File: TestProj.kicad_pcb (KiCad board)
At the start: 2 copper layers, 24 parts, among them SW1 SW_Push, U1 ATmega32U4-AU, Y1 16MHz

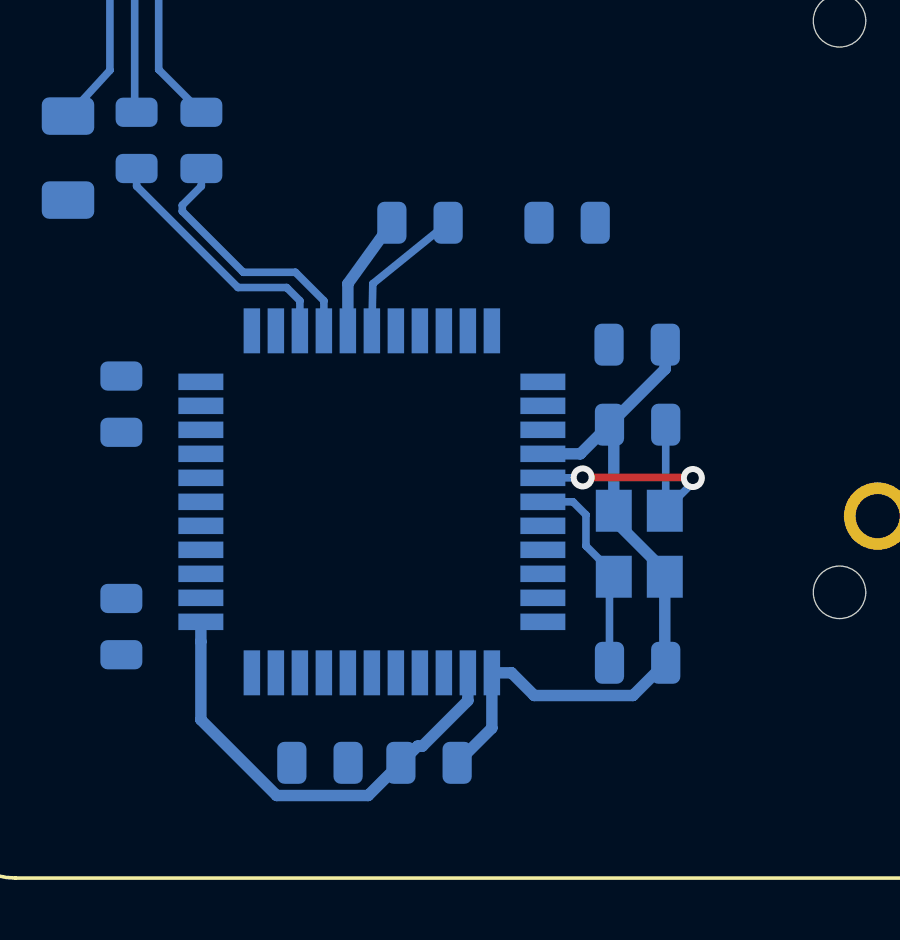
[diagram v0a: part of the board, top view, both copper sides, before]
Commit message: early pcb routing
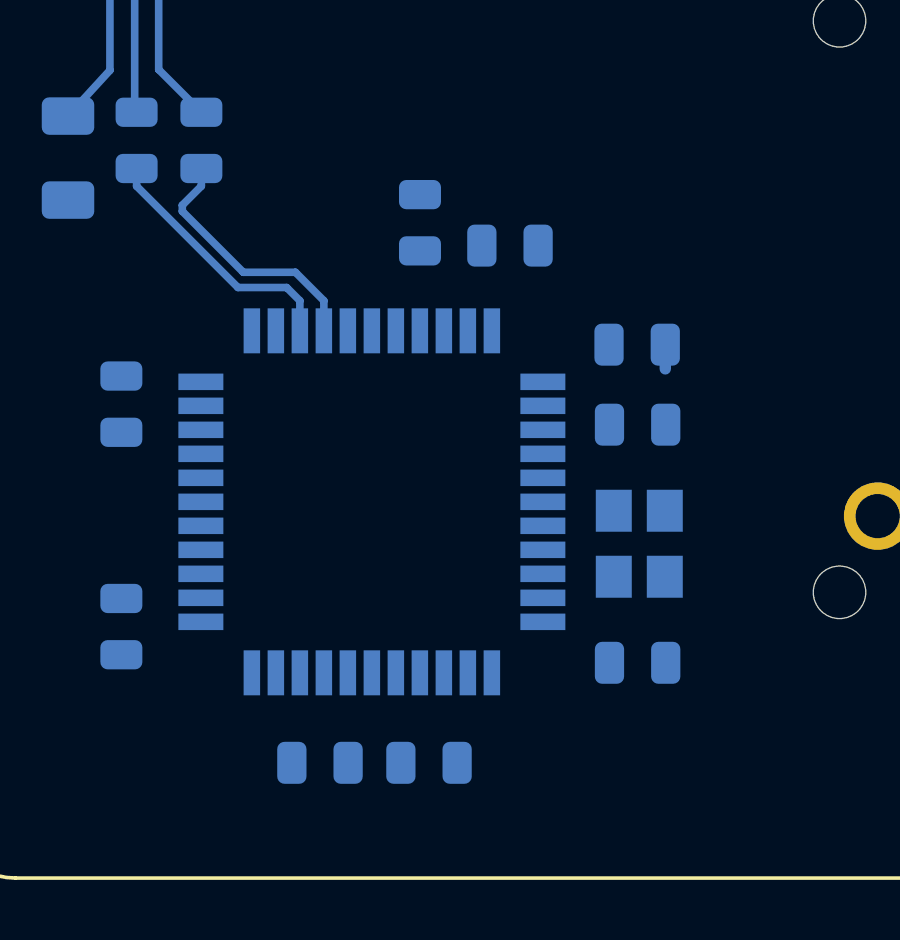
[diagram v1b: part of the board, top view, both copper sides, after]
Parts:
- moved R3 2.05 mm to (106.2, 105.9)
- turned C7 to 90 degrees
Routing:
- net GND: track 28.9 -> 1.55 mm
- net +5V: track 15.4 -> 0.00 mm
- net Net-(C4-Pad1): track 9.37 -> 0.04 mm, vias 2 -> 0
- net Net-(C3-Pad1): track 6.99 -> 0.30 mm
- net Net-(C7-Pad1): track 4.80 -> 0.00 mm
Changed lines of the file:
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@@
     (thickness 1.6)
     (drawings 8)
-    (tracks 67)
+    (tracks 28)
     (zones 0)
     (modules 24)
@@
   )
   (module Resistor_SMD:R_0805_2012Metric (layer B.Cu)
-    (at 108.077 105.156 180)
+    (at 106.172 105.918 180)
     (descr "Resistor SMD 0805 (2012 Metric), square (rectangular) end terminal, IPC_7351 nominal, (Body size source: https://docs.google.com/spreadsheets/d/1BsfQQcO9C6DZCsRaXUlFlo91Tg2WpOkGARC1WS5S8t0/edit?usp=sharing), generated with kicad-footprint-generator")
     (tags resistor)
@@
   )
   (module Capacitor_SMD:C_0805_2012Metric (layer B.Cu)
-    (at 103.1725 105.156 180)
+    (at 103.1725 105.156 90)
     (descr "Capacitor SMD 0805 (2012 Metric), square (rectangular) end terminal, IPC_7351 nominal, (Body size source: https://docs.google.com/spreadsheets/d/1BsfQQcO9C6DZCsRaXUlFlo91Tg2WpOkGARC1WS5S8t0/edit?usp=sharing), generated with kicad-footprint-generator")
     (tags capacitor)
     (attr smd)
-    (fp_text reference C7 (at 0 1.65) (layer B.SilkS)
-      (effects (font (size 1 1) (thickness 0.15)) (justify mirror))
-    )
-    (fp_text value 1uF (at 0 -1.65) (layer B.Fab)
-      (effects (font (size 1 1) (thickness 0.15)) (justify mirror))
-    )
-    (fp_text user %R (at 0 0) (layer B.Fab)
+    (fp_text reference C7 (at 0 1.65 90) (layer B.SilkS)
+      (effects (font (size 1 1) (thickness 0.15)) (justify mirror))
+    )
+    (fp_text value 1uF (at 0 -1.65 90) (layer B.Fab)
+      (effects (font (size 1 1) (thickness 0.15)) (justify mirror))
+    )
+    (fp_text user %R (at 0 0 90) (layer B.Fab)
       (effects (font (size 0.5 0.5) (thickness 0.08)) (justify mirror))
     )
@@
     (fp_line (start -1 0.6) (end 1 0.6) (layer B.Fab) (width 0.1))
     (fp_line (start -1 -0.6) (end -1 0.6) (layer B.Fab) (width 0.1))
-    (pad 2 smd roundrect (at 0.9375 0 180) (size 0.975 1.4) (layers B.Cu B.Paste B.Mask) (roundrect_rratio 0.25)
-      (net 1 GND))
-    (pad 1 smd roundrect (at -0.9375 0 180) (size 0.975 1.4) (layers B.Cu B.Paste B.Mask) (roundrect_rratio 0.25)
+    (pad 2 smd roundrect (at 0.9375 0 90) (size 0.975 1.4) (layers B.Cu B.Paste B.Mask) (roundrect_rratio 0.25)
+      (net 1 GND))
+    (pad 1 smd roundrect (at -0.9375 0 90) (size 0.975 1.4) (layers B.Cu B.Paste B.Mask) (roundrect_rratio 0.25)
       (net 5 "Net-(C7-Pad1)"))
     (model ${KISYS3DMOD}/Capacitor_SMD.3dshapes/C_0805_2012Metric.wrl
@@
   (gr_arc (start 148.43125 124.61875) (end 148.43125 127) (angle -90) (layer F.SilkS) (width 0.12))
   (gr_arc (start 148.43125 91.28125) (end 150.8125 91.28125) (angle -90) (layer F.SilkS) (width 0.12))
-  (segment (start 100.76825 107.188) (end 100.76825 108.75875) (width 0.381) (layer B.Cu) (net 1))
-  (segment (start 102.235 105.156) (end 100.76825 107.188) (width 0.381) (layer B.Cu) (net 1))
-  (segment (start 109.63275 115.058652) (end 111.33275 116.758652) (width 0.381) (layer B.Cu) (net 1))
   (segment (start 111.33275 116.758652) (end 111.33275 116.95575) (width 0.381) (layer B.Cu) (net 1))
   (segment (start 109.63275 114.75575) (end 109.63275 115.058652) (width 0.381) (layer B.Cu) (net 1))
   (segment (start 109.63275 112.03075) (end 109.489 111.887) (width 0.381) (layer B.Cu) (net 1))
-  (segment (start 109.63275 114.75575) (end 109.63275 112.03075) (width 0.381) (layer B.Cu) (net 1))
-  (segment (start 108.51725 112.85875) (end 107.26825 112.85875) (width 0.381) (layer B.Cu) (net 1))
-  (segment (start 109.489 111.887) (end 108.51725 112.85875) (width 0.381) (layer B.Cu) (net 1))
-  (segment (start 111.349 110.027) (end 109.489 111.887) (width 0.381) (layer B.Cu) (net 1))
   (segment (start 111.349 109.22) (end 111.349 110.027) (width 0.381) (layer B.Cu) (net 1))
   (segment (start 111.33275 119.79325) (end 111.364 119.8245) (width 0.381) (layer B.Cu) (net 1))
-  (segment (start 111.33275 116.95575) (end 111.33275 119.79325) (width 0.381) (layer B.Cu) (net 1))
-  (segment (start 106.22425 120.15875) (end 105.56825 120.15875) (width 0.381) (layer B.Cu) (net 1))
-  (segment (start 106.98051 120.91501) (end 106.22425 120.15875) (width 0.381) (layer B.Cu) (net 1))
-  (segment (start 110.27349 120.91501) (end 106.98051 120.91501) (width 0.381) (layer B.Cu) (net 1))
-  (segment (start 111.364 119.8245) (end 110.27349 120.91501) (width 0.381) (layer B.Cu) (net 1))
-  (segment (start 105.56825 122.00075) (end 105.56825 120.15875) (width 0.381) (layer B.Cu) (net 1))
-  (segment (start 104.41075 123.15825) (end 105.56825 122.00075) (width 0.381) (layer B.Cu) (net 1))
-  (segment (start 103.091987 122.602013) (end 103.252889 122.602013) (width 0.381) (layer B.Cu) (net 2))
-  (segment (start 104.76825 121.086652) (end 104.76825 120.15875) (width 0.381) (layer B.Cu) (net 2))
-  (segment (start 103.252889 122.602013) (end 104.76825 121.086652) (width 0.381) (layer B.Cu) (net 2))
-  (segment (start 102.53575 123.15825) (end 103.091987 122.602013) (width 0.381) (layer B.Cu) (net 2))
-  (segment (start 95.86825 119.11475) (end 95.86825 118.45875) (width 0.381) (layer B.Cu) (net 2))
-  (segment (start 95.86825 121.72223) (end 95.86825 119.11475) (width 0.381) (layer B.Cu) (net 2))
-  (segment (start 98.39478 124.24876) (end 95.86825 121.72223) (width 0.381) (layer B.Cu) (net 2))
-  (segment (start 101.44524 124.24876) (end 98.39478 124.24876) (width 0.381) (layer B.Cu) (net 2))
-  (segment (start 102.53575 123.15825) (end 101.44524 124.24876) (width 0.381) (layer B.Cu) (net 2))
-  (segment (start 108.705749 115.928749) (end 109.63275 116.85575) (width 0.254) (layer B.Cu) (net 3))
-  (segment (start 108.705749 114.892249) (end 108.705749 115.928749) (width 0.254) (layer B.Cu) (net 3))
-  (segment (start 108.27225 114.45875) (end 108.705749 114.892249) (width 0.254) (layer B.Cu) (net 3))
   (segment (start 109.63275 116.85575) (end 109.63275 116.95575) (width 0.254) (layer B.Cu) (net 3))
-  (segment (start 107.26825 114.45875) (end 108.27225 114.45875) (width 0.254) (layer B.Cu) (net 3))
   (segment (start 109.489 117.0995) (end 109.63275 116.95575) (width 0.254) (layer B.Cu) (net 3))
-  (segment (start 109.489 119.8245) (end 109.489 117.0995) (width 0.254) (layer B.Cu) (net 3))
   (segment (start 111.364 114.7245) (end 111.33275 114.75575) (width 0.254) (layer B.Cu) (net 4))
-  (segment (start 111.364 111.887) (end 111.364 114.7245) (width 0.254) (layer B.Cu) (net 4))
-  (segment (start 108.581664 113.65875) (end 108.594996 113.645418) (width 0.254) (layer B.Cu) (net 4))
-  (via (at 108.594996 113.645418) (size 0.8) (drill 0.4) (layers F.Cu B.Cu) (net 4))
-  (segment (start 107.26825 113.65875) (end 108.581664 113.65875) (width 0.254) (layer B.Cu) (net 4))
-  (via (at 112.268 113.665) (size 0.8) (drill 0.4) (layers F.Cu B.Cu) (net 4))
-  (segment (start 112.248418 113.645418) (end 112.268 113.665) (width 0.254) (layer F.Cu) (net 4))
-  (segment (start 108.594996 113.645418) (end 112.248418 113.645418) (width 0.254) (layer F.Cu) (net 4))
-  (segment (start 112.268 113.8205) (end 111.33275 114.75575) (width 0.254) (layer B.Cu) (net 4))
-  (segment (start 112.268 113.665) (end 112.268 113.8205) (width 0.254) (layer B.Cu) (net 4))
-  (segment (start 101.6 107.188) (end 101.56825 108.75875) (width 0.254) (layer B.Cu) (net 5))
-  (segment (start 104.11 105.156) (end 101.6 107.188) (width 0.254) (layer B.Cu) (net 5))
   (segment (start 92.837 96.6545) (end 92.837 100.076) (width 0.254) (layer B.Cu) (net 12))
   (segment (start 92.8625 96.629) (end 92.837 96.6545) (width 0.254) (layer B.Cu) (net 12))

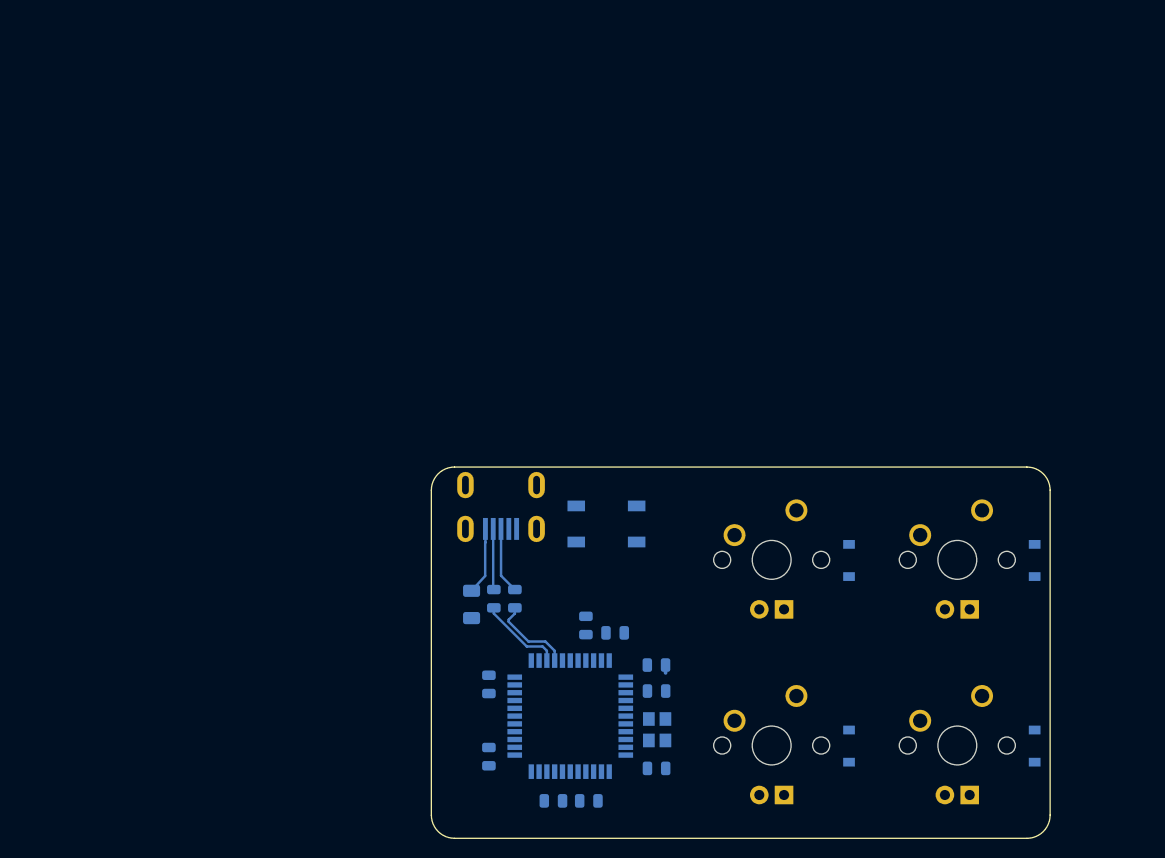
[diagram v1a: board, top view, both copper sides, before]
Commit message: starting from scratch with atmega32u2
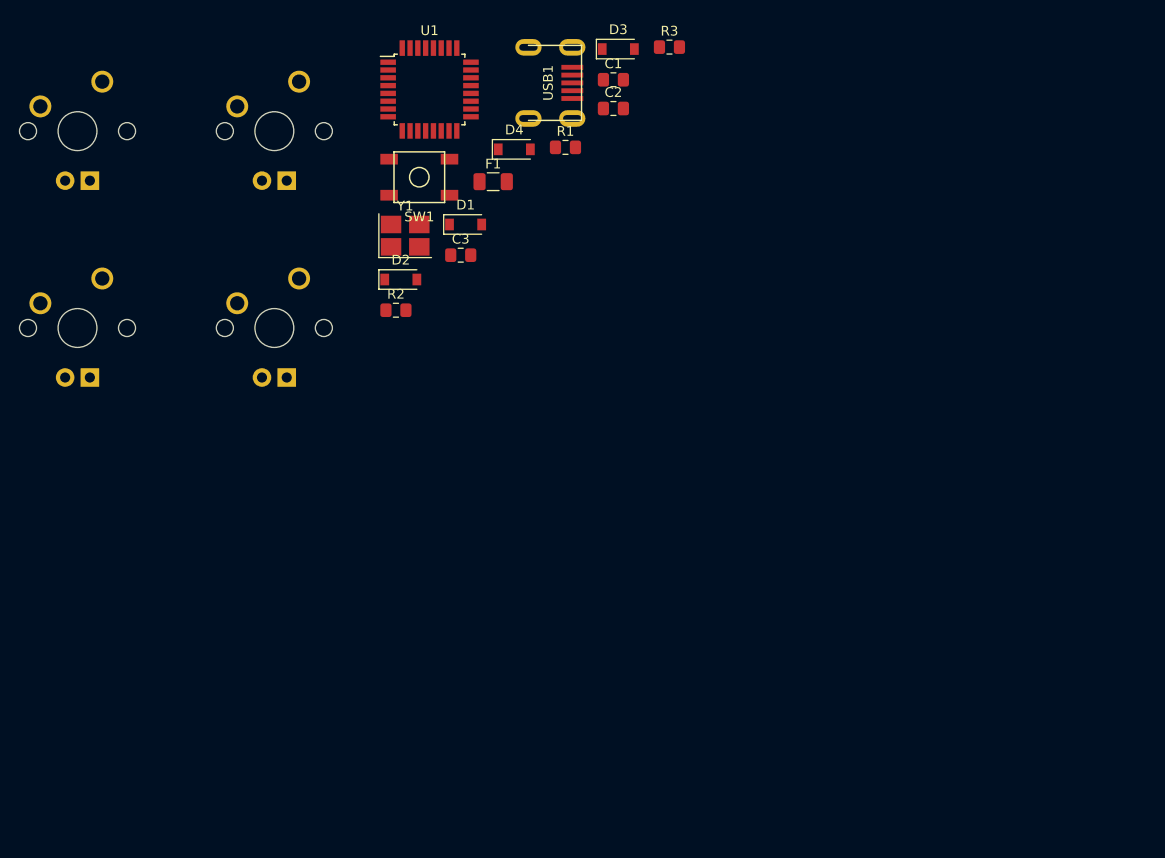
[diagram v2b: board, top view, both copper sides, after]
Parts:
- removed C4: 22pF, Capacitor_SMD:C_0805_2012Metric
- removed C5: 0.1uF, Capacitor_SMD:C_0805_2012Metric
- removed C6: 10uF, Capacitor_SMD:C_0805_2012Metric
- removed C7: 1uF, Capacitor_SMD:C_0805_2012Metric
- removed R4: 10k, Resistor_SMD:R_0805_2012Metric
- C1, C2: value 0.1uF -> 22pF; footprint Capacitor_SMD:C_0805_2012Metric -> Capacitor_SMD:C_0805_2012Metric_Pad1.15x1.40mm_HandSolder; moved to F.Cu
- C3: value 22pF -> 1uF; footprint Capacitor_SMD:C_0805_2012Metric -> Capacitor_SMD:C_0805_2012Metric_Pad1.15x1.40mm_HandSolder; moved to F.Cu
- D1, D2, D3, D4, F1, SW1, USB1: moved to F.Cu
- R1, R2, R3: footprint Resistor_SMD:R_0805_2012Metric -> Resistor_SMD:R_0805_2012Metric_Pad1.15x1.40mm_HandSolder; moved to F.Cu
- U1: value ATmega32U4-AU -> ATmega32U2-AU; footprint Package_QFP:TQFP-44_10x10mm_P0.8mm -> Package_QFP:TQFP-32_7x7mm_P0.8mm; moved to F.Cu
- Y1: footprint Crystal:Crystal_SMD_3225-4Pin_3.2x2.5mm -> Crystal:Crystal_SMD_3225-4Pin_3.2x2.5mm_HandSoldering; moved to F.Cu
- moved MX2 95.1 mm to (51.0, 54.4)
- moved MX3 82.7 mm to (71.2, 54.4)
- moved MX4 82.1 mm to (71.2, 74.6)
- moved D4 81.3 mm to (95.8, 56.3), turned to 0 degrees
- moved MX1 75.1 mm to (51.0, 74.6)
- moved C2 71.1 mm to (106.0, 52.1)
- moved D3 67.7 mm to (106.5, 46.0), turned to 0 degrees
- moved D2 66.4 mm to (84.2, 69.7), turned to 0 degrees
- moved U1 65.9 mm to (87.1, 50.2), turned to 0 degrees
- moved R3 60.4 mm to (111.7, 45.8), turned to 0 degrees
- moved C1 60.2 mm to (106.0, 49.2)
- moved Y1 56.9 mm to (84.6, 65.2), turned to 0 degrees
- moved C3 56.4 mm to (90.3, 67.2)
- moved D1 52.3 mm to (90.8, 64.0), turned to 0 degrees
- moved R1 46.9 mm to (101.1, 56.1), turned to 0 degrees
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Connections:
- C1 pad 1: +5V -> Net-(C1-Pad1)
- C2 pad 1: +5V -> GND
- C2 pad 2: GND -> Net-(C2-Pad2)
- R1 pad 1: Net-(R1-Pad1) -> D-
- R1 pad 2: D- -> Net-(R1-Pad2)
- U1 pad 1: Net-(U1-Pad1) -> Net-(C1-Pad1)
- U1 pad 13: Net-(R3-Pad2) -> Net-(U1-Pad13)
- U1 pad 14: +5V -> Net-(U1-Pad14)
- U1 pad 15: GND -> Net-(U1-Pad15)
- U1 pad 16: Net-(C4-Pad1) -> Net-(U1-Pad16)
- U1 pad 17: Net-(C3-Pad1) -> Net-(U1-Pad17)
- U1 pad 2: +5V -> Net-(C2-Pad2)
- U1 pad 23: GND -> Net-(U1-Pad23)
- U1 pad 24: +5V -> Net-(R3-Pad2)
- U1 pad 27: Net-(U1-Pad27) -> Net-(C3-Pad1)
- U1 pad 28: Net-(U1-Pad28) -> GND
- U1 pad 29: Net-(U1-Pad29) -> Net-(R2-Pad1)
- U1 pad 3: Net-(R1-Pad1) -> GND
- U1 pad 30: Net-(U1-Pad30) -> Net-(R1-Pad2)
- U1 pad 31: Net-(U1-Pad31) -> +5V
- U1 pad 32: Net-(U1-Pad32) -> +5V
- U1 pad 4: Net-(R2-Pad1) -> +5V
- U1 pad 5: GND -> Net-(U1-Pad5)
- U1 pad 7: +5V -> Net-(U1-Pad7)
- Y1 pad 1: Net-(C4-Pad1) -> Net-(C1-Pad1)
- Y1 pad 3: Net-(C3-Pad1) -> Net-(C2-Pad2)
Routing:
- net Net-(R2-Pad1): track 8.65 -> 0.00 mm
- net Net-(R1-Pad1): track 8.62 -> 0.00 mm
- net VCC: track 6.90 -> 0.00 mm
- net D+: track 6.81 -> 0.00 mm
- net D-: track 6.25 -> 0.00 mm
- net GND: track 1.55 -> 0.00 mm

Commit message: a poor routing job 8)
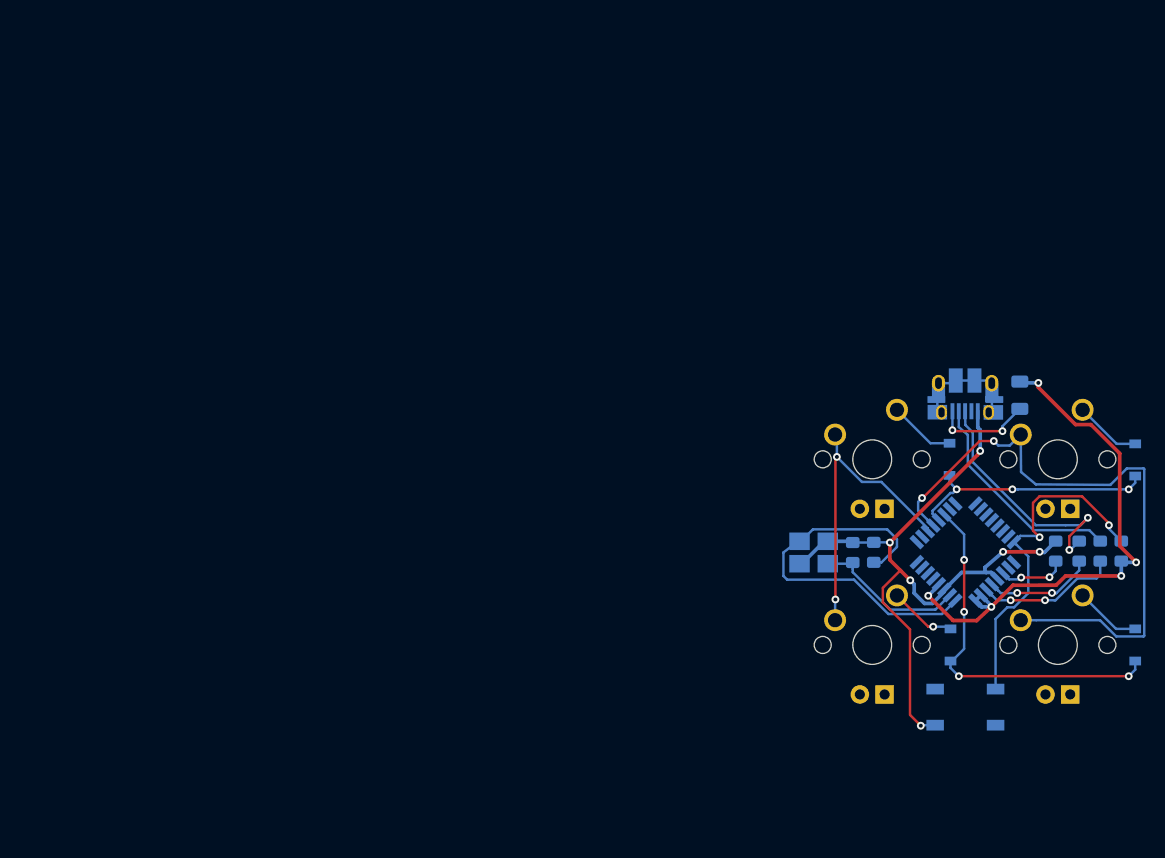
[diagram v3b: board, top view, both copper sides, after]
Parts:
- removed F1: 500mA, Fuse:Fuse_1206_3216Metric
- removed USB1: Molex-0548190589, random-keyboard-parts:Molex-0548190589
- added F2: 500mA, Fuse:Fuse_1206_3216Metric, B.Cu at (147.7, 81.5)
- added J1: USB_B_Micro, Connector_USB:USB_Micro-B_Amphenol_10103594-0001LF_Horizontal, B.Cu at (142.1, 81.4)
- C1, C2, C3, D1, D2, D3, D4, R1, R2, R3, U1, Y1: moved to B.Cu
- SW1: footprint random-keyboard-parts:SKQG-1155865 -> random-keyboard-parts:SKQGADE010; moved to B.Cu
- moved MX2 97.1 mm to (132.6, 107.2)
- moved MX3 87.2 mm to (151.6, 88.1)
- moved MX4 86.7 mm to (151.6, 107.2)
- moved MX1 82.7 mm to (132.6, 88.1)
- moved D4 81.5 mm to (159.5, 107.2), turned to 90 degrees
- moved SW1 78.1 mm to (142.1, 113.5), turned to 180 degrees
- moved R2 74.4 mm to (153.8, 97.5), turned to 90 degrees
- moved U1 72.6 mm to (142.1, 97.6), turned to 45 degrees
- moved R3 69.5 mm to (158.1, 97.5), turned to 90 degrees
- moved R1 68.8 mm to (156.0, 97.5), turned to 270 degrees
- moved C3 68.2 mm to (151.4, 97.5), turned to 90 degrees
- moved D3 67.8 mm to (159.5, 88.2), turned to 90 degrees
- moved D2 67.7 mm to (140.6, 107.2), turned to 90 degrees
- moved C1 55.4 mm to (132.7, 97.7), turned to 90 degrees
- moved D1 55.2 mm to (140.5, 88.1), turned to 90 degrees
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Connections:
- U1 pad 11: Net-(U1-Pad11) -> COL0
- U1 pad 12: Net-(U1-Pad12) -> COL1
- U1 pad 13: Net-(U1-Pad13) -> ROW0
- U1 pad 14: Net-(U1-Pad14) -> ROW1
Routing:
- net GND: track 0.00 -> 73.4 mm, vias 0 -> 6
- net COL1: track 0.00 -> 65.0 mm, vias 0 -> 2
- net +5V: track 0.00 -> 57.1 mm, vias 0 -> 5
- net Net-(C1-Pad1): track 0.00 -> 39.0 mm
- net ROW1: track 0.00 -> 37.7 mm, vias 0 -> 4
- net Net-(R3-Pad2): track 0.00 -> 35.8 mm, vias 0 -> 2
- net COL0: track 0.00 -> 31.9 mm, vias 0 -> 2
- net D+: track 0.00 -> 25.8 mm, vias 0 -> 2
- net ROW0: track 0.00 -> 25.6 mm, vias 0 -> 3
- net D-: track 0.00 -> 22.7 mm
- net Net-(C2-Pad2): track 0.00 -> 15.8 mm
- net Net-(R1-Pad2): track 0.00 -> 14.6 mm, vias 0 -> 2
- net Net-(R2-Pad1): track 0.00 -> 12.3 mm, vias 0 -> 2
- net VCC: track 0.00 -> 10.1 mm, vias 0 -> 2
- net Net-(J1-Pad6): track 0.00 -> 9.23 mm
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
